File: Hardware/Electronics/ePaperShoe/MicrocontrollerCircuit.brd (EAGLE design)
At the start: 160 x 100 mm, 22 parts, among them U2 NRF52832, X1 32MHz, X2 32.768kHz

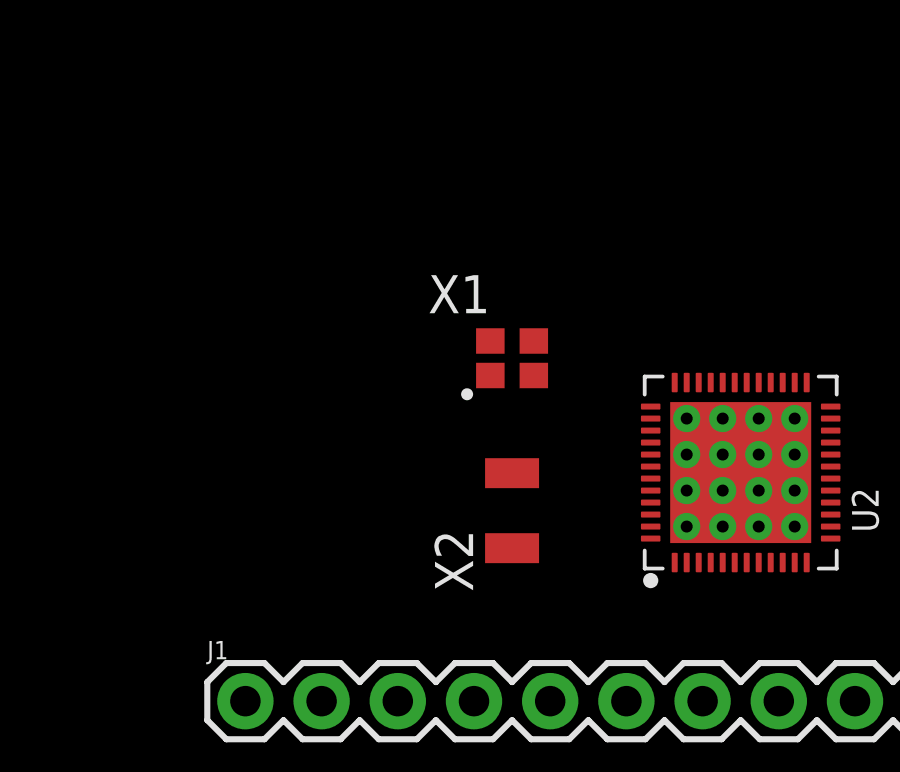
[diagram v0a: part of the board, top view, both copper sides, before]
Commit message: Minor adjustments to the to nRF52 PCB
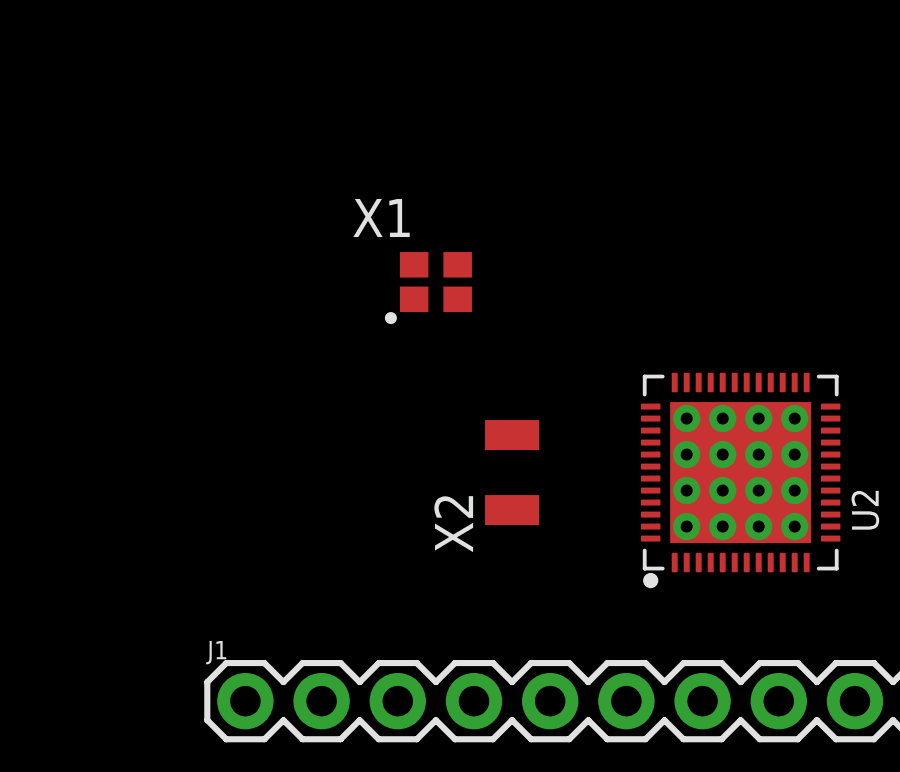
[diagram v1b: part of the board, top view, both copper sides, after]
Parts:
- moved X1 3.59 mm to (34.3, 16.5)
- moved X2 1.27 mm to (36.8, 10.2)
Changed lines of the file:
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@@
 <element name="U2" library="Nordic_nRF" package="QFN40P600X600X90-48_N" value="NRF52832" x="44.45" y="10.16" rot="R90"/>
 <element name="UC_LED" library="microbuilder" package="CHIPLED_0805_NOOUTLINE" value="ORANGE" x="60.96" y="11.43"/>
-<element name="X1" library="Nordic_nRF" package="BT-XTAL_2016_N" value="32MHz" x="36.83" y="13.97"/>
-<element name="X2" library="Nordic_nRF" package="XTAL_3215_N" value="32.768kHz" x="36.83" y="8.89" rot="R90"/>
+<element name="X1" library="Nordic_nRF" package="BT-XTAL_2016_N" value="32MHz" x="34.29" y="16.51"/>
+<element name="X2" library="Nordic_nRF" package="XTAL_3215_N" value="32.768kHz" x="36.83" y="10.16" rot="R90"/>
 <element name="C1" library="microbuilder" package="1206" value="12pF" x="-19.05" y="15.24"/>
 <element name="C2" library="microbuilder" package="1206" value="12pF" x="-11.43" y="96.52"/>
@@
 <wire x1="-12.83" y1="96.52" x2="-10.03" y2="90.17" width="0" layer="19" extent="1-1"/>
 <wire x1="-20.45" y1="15.24" x2="-12.83" y2="96.52" width="0" layer="19" extent="1-1"/>
-<wire x1="36.105" y1="14.545" x2="-20.45" y2="15.24" width="0" layer="19" extent="1-1"/>
-<wire x1="37.555" y1="13.395" x2="36.105" y2="14.545" width="0" layer="19" extent="1-1"/>
-<wire x1="42.65" y1="11.96" x2="37.555" y2="13.395" width="0" layer="19" extent="1-1"/>
+<wire x1="33.565" y1="17.085" x2="-20.45" y2="15.24" width="0" layer="19" extent="1-1"/>
+<wire x1="35.015" y1="15.935" x2="33.565" y2="17.085" width="0" layer="19" extent="1-1"/>
+<wire x1="42.65" y1="11.96" x2="35.015" y2="15.935" width="0" layer="19" extent="1-1"/>
 <wire x1="43.85" y1="11.96" x2="42.65" y2="11.96" width="0" layer="19" extent="1-1"/>
 <wire x1="43.85" y1="10.76" x2="43.85" y2="11.96" width="0" layer="19" extent="1-1"/>
@@
 <contactref element="U2" pad="35"/>
 <contactref element="C1" pad="2"/>
-<wire x1="37.555" y1="14.545" x2="42.65" y2="13.16" width="0" layer="19" extent="1-1"/>
-<wire x1="-17.65" y1="15.24" x2="37.555" y2="14.545" width="0" layer="19" extent="1-1"/>
+<wire x1="35.015" y1="17.085" x2="42.65" y2="13.16" width="0" layer="19" extent="1-1"/>
+<wire x1="-17.65" y1="15.24" x2="35.015" y2="17.085" width="0" layer="19" extent="1-1"/>
 </signal>
 <signal name="X1">
@@
 <contactref element="U2" pad="34"/>
 <contactref element="C2" pad="2"/>
-<wire x1="36.105" y1="13.395" x2="43.05" y2="13.16" width="0" layer="19" extent="1-1"/>
-<wire x1="-10.03" y1="96.52" x2="36.105" y2="13.395" width="0" layer="19" extent="1-1"/>
+<wire x1="33.565" y1="15.935" x2="43.05" y2="13.16" width="0" layer="19" extent="1-1"/>
+<wire x1="-10.03" y1="96.52" x2="33.565" y2="15.935" width="0" layer="19" extent="1-1"/>
 </signal>
 <signal name="P0.31">
@@
 <contactref element="U2" pad="2"/>
 <contactref element="C10" pad="1"/>
-<wire x1="36.83" y1="7.64" x2="-12.83" y2="45.72" width="0" layer="19" extent="1-1"/>
-<wire x1="42.65" y1="7.16" x2="36.83" y2="7.64" width="0" layer="19" extent="1-1"/>
+<wire x1="36.83" y1="8.91" x2="-12.83" y2="45.72" width="0" layer="19" extent="1-1"/>
+<wire x1="42.65" y1="7.16" x2="36.83" y2="8.91" width="0" layer="19" extent="1-1"/>
 </signal>
 <signal name="P0.01">
@@
 <contactref element="U2" pad="3"/>
 <contactref element="C11" pad="1"/>
-<wire x1="36.83" y1="10.14" x2="-12.83" y2="39.37" width="0" layer="19" extent="1-1"/>
-<wire x1="43.05" y1="7.16" x2="36.83" y2="10.14" width="0" layer="19" extent="1-1"/>
+<wire x1="36.83" y1="11.41" x2="-12.83" y2="39.37" width="0" layer="19" extent="1-1"/>
+<wire x1="43.05" y1="7.16" x2="36.83" y2="11.41" width="0" layer="19" extent="1-1"/>
 </signal>
 <signal name="SWDCLK">

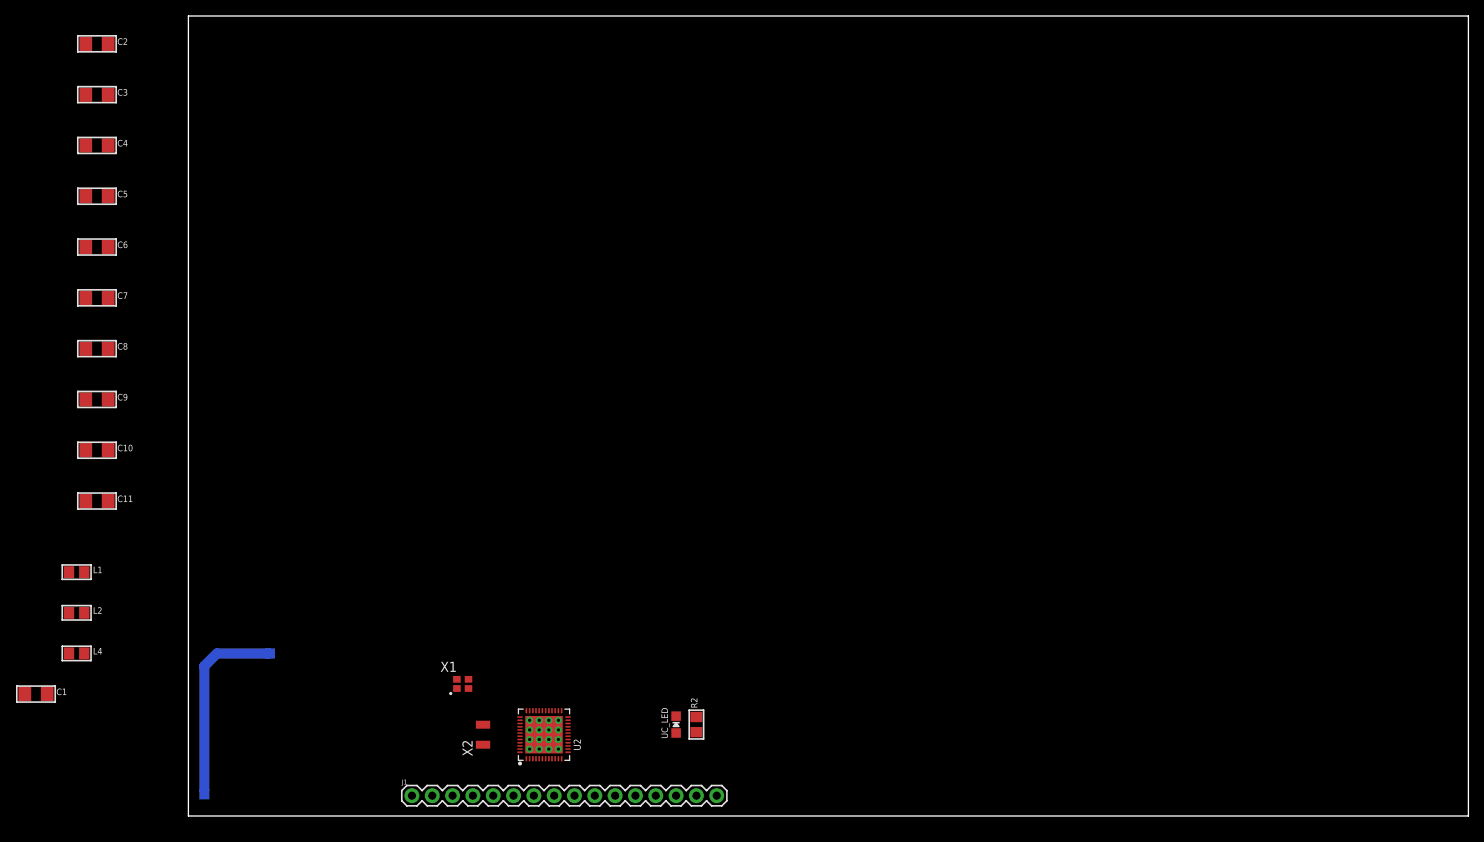
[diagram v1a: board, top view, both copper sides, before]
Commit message: Finished design of microcontroller circuit and added logic analyser snapshots
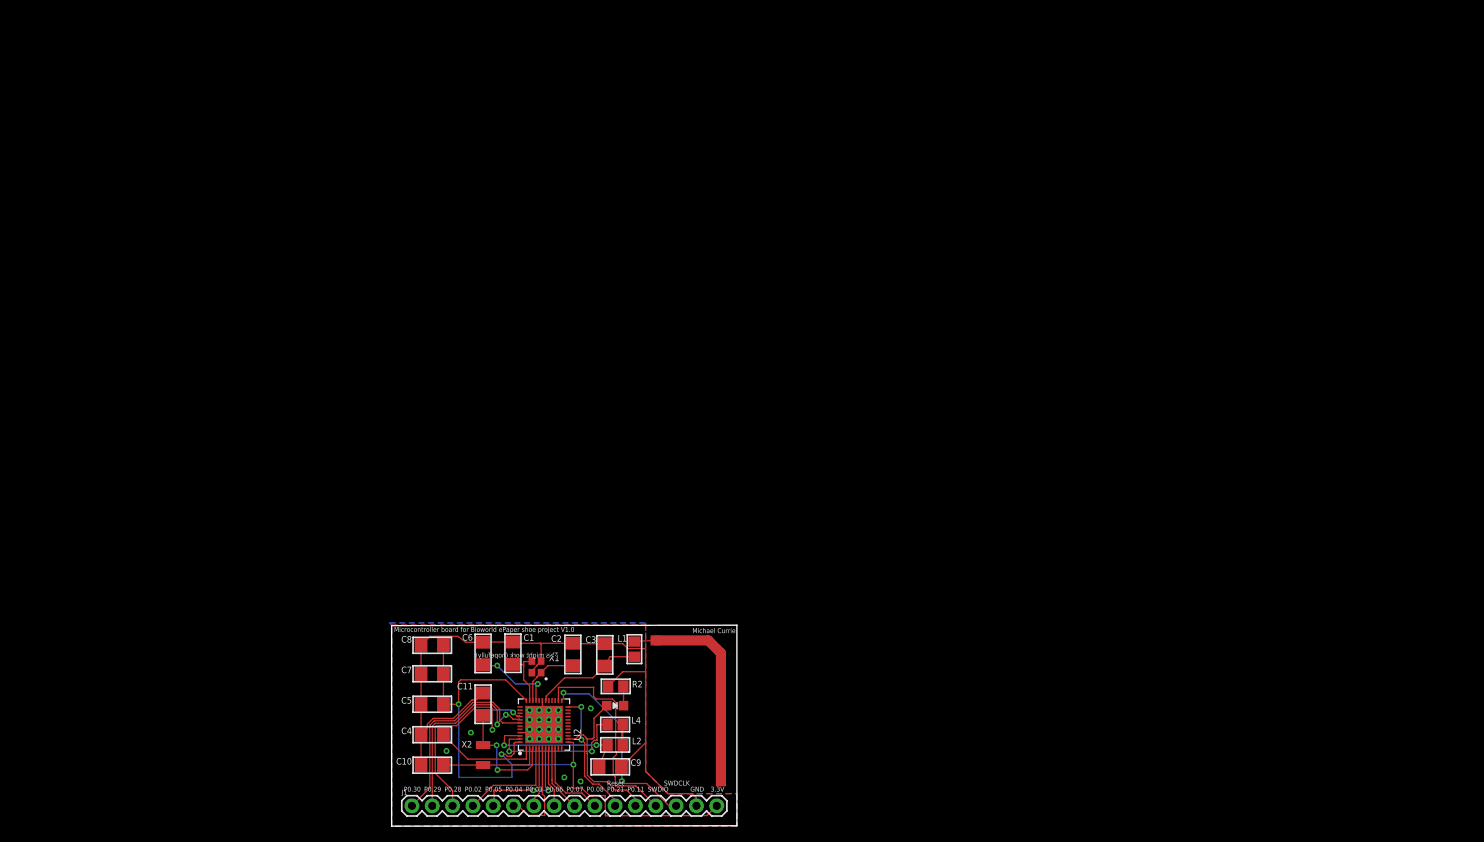
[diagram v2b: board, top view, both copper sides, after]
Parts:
- moved C2 96.8 mm to (48.1, 20.2), turned to 270 degrees
- moved C3 94.5 mm to (52.0, 20.1), turned to 90 degrees
- moved C4 84.7 mm to (30.5, 10.2), turned to 180 degrees
- moved C9 78.9 mm to (52.7, 6.15)
- moved C5 76.1 mm to (30.5, 14.0), turned to 180 degrees
- moved L1 70.4 mm to (55.8, 20.9), turned to 90 degrees
- moved C6 70.1 mm to (36.8, 20.3), turned to 90 degrees
- moved L2 69.3 mm to (53.3, 8.89), turned to 180 degrees
- moved L4 67.9 mm to (53.3, 11.4)
- moved C7 63.0 mm to (30.5, 17.8), turned to 180 degrees
- moved C1 59.8 mm to (40.6, 20.3), turned to 270 degrees
- moved C10 57.5 mm to (30.5, 6.35), turned to 180 degrees
- moved C8 56.0 mm to (30.5, 21.3), turned to 180 degrees
- moved C11 54.5 mm to (36.8, 14.0), turned to 90 degrees
- moved FRAME2 48.7 mm to (27.9, 44.5), turned to 270 degrees
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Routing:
- net GND: track 0.00 -> 125.7 mm, vias 0 -> 5
- net 3.3V: track 0.00 -> 80.2 mm, vias 0 -> 3
- net P0.28: track 0.00 -> 28.0 mm, vias 0 -> 2
- net SWDIO: track 0.00 -> 27.1 mm
- net P0.30: track 0.00 -> 25.3 mm
- net SWDCLK: track 0.00 -> 25.0 mm, vias 0 -> 2
- net P0.29: track 0.00 -> 24.9 mm, vias 0 -> 2
- net P0.11: track 0.00 -> 21.1 mm
- net DEC4: track 0.00 -> 19.0 mm, vias 0 -> 2
- net N$5: track 0.00 -> 18.4 mm, vias 0 -> 2
- net P0.21/RESET: track 0.00 -> 16.2 mm, vias 0 -> 2
- net P0.01/XL2: track 0.00 -> 15.2 mm, vias 0 -> 2
- net P0.05: track 0.00 -> 14.2 mm, vias 0 -> 2
- net ANT: track 0.00 -> 13.8 mm
- net P0.02: track 0.00 -> 13.5 mm
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- added copper zone on layer 1, net GND
- added copper zone on layer 16, net GND
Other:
- board size 160 x 100 mm -> 43.2 x 25.1 mm
- board text added: "3.3V"
- board text added: "Always Listening"
- board text added: "GND"
- board text added: "Michael Currie"
- board text added: "Microcontroller board for Bioworld ePaper shoe project V1.0"
- board text added: "P0.02"
- board text added: "P0.03"
- board text added: "P0.04"
- board text added: "P0.05"
- board text added: "P0.06"
- board text added: "P0.07"
- board text added: "P0.08"
- board text added: "P0.11"
- board text added: "P0.21"
- board text added: "P0.28"
- board text added: "P0.29"
- board text added: "P0.30"
- board text added: "Reset"
- board text added: "SWDCLK"
- board text added: "SWDIO"
- board text added: "This might work (hopefully)"
- board text added: "WARNING"
